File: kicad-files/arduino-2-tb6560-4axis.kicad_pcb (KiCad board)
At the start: 2 copper layers, 55.9 x 63.5 mm, 16 parts, among them J1 DB25_Female_MountingHoles, J2 Conn_01x03_Male, J3 Conn_01x02_Male, J4 Conn_01x02_Male, J5 Conn_01x03_Male, J6 Conn_01x02_Male, J7 Conn_01x03_Male, Q1 2N3904

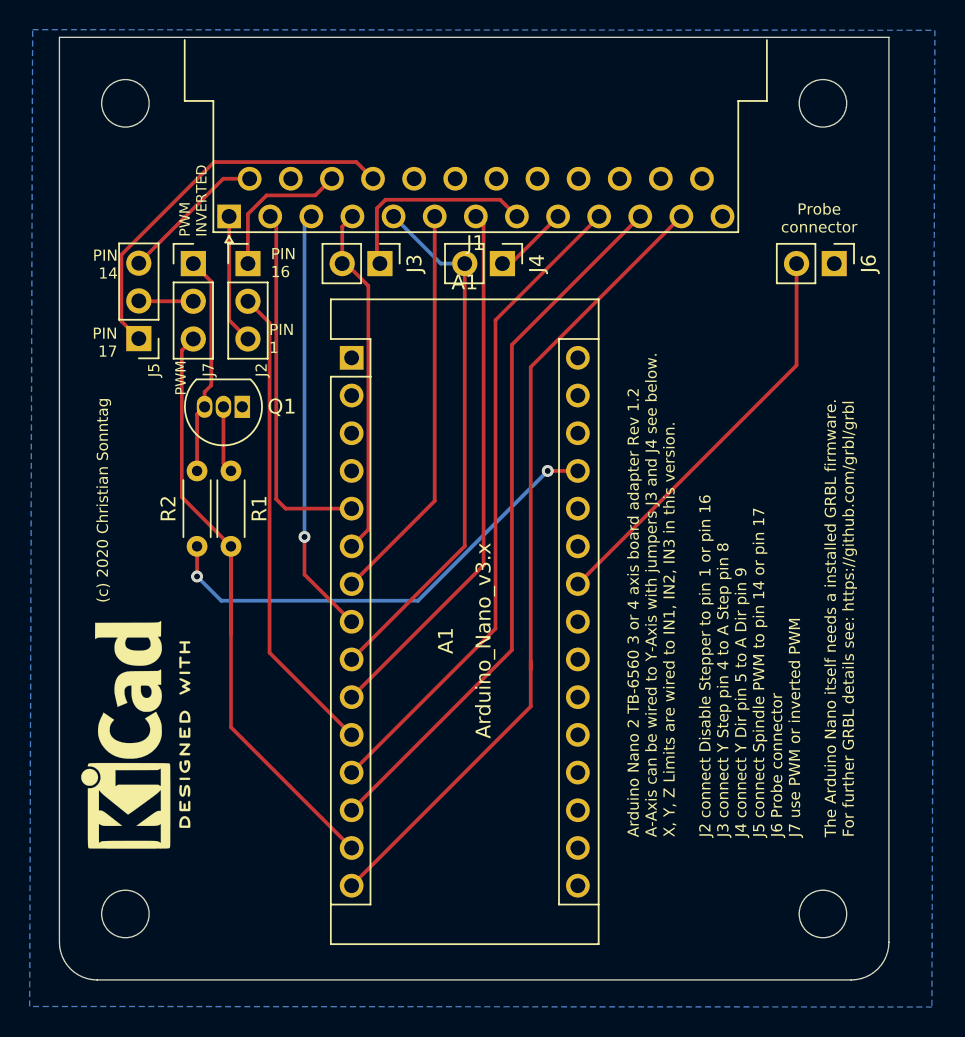
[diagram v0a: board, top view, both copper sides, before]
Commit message: added push buttons and jumper header for feed hold and cycle start/resume.
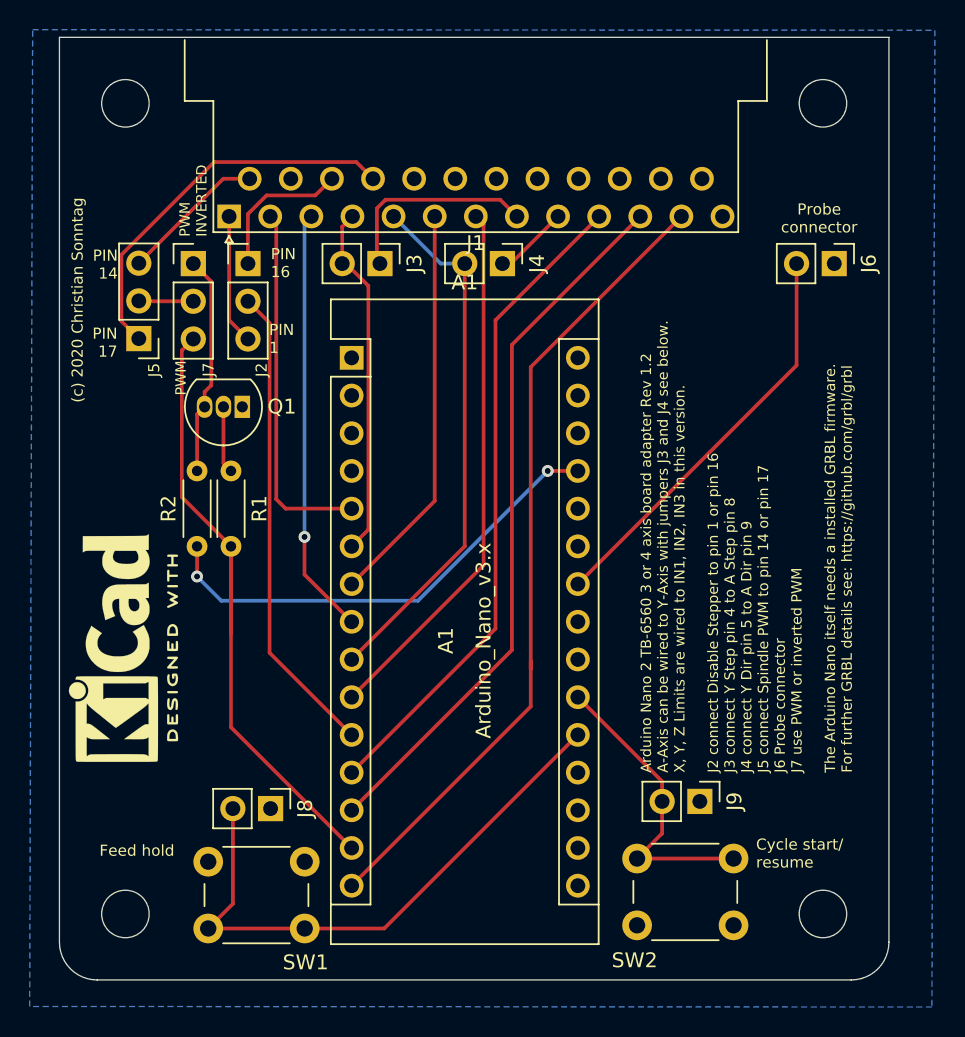
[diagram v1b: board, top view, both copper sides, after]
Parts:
- added J8: Conn_01x02_Male, Connector_PinHeader_2.54mm:PinHeader_1x02_P2.54mm_Vertical, F.Cu at (140.6, 96.4)
- added J9: Conn_01x02_Male, Connector_PinHeader_2.54mm:PinHeader_1x02_P2.54mm_Vertical, F.Cu at (169.5, 95.9)
- added SW1: SW_Push, Button_Switch_THT:SW_PUSH_6mm_H7.3mm, F.Cu at (142.9, 104.5)
- added SW2: SW_Push, Button_Switch_THT:SW_PUSH_6mm_H7.3mm, F.Cu at (165.3, 99.8)
- moved REF** 5.90 mm to (130.0, 85.6)
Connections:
- A1 pad 20: Net-(A1-Pad20) -> FEED_HOLD
- A1 pad 21: Net-(A1-Pad21) -> CYCLE_START_RESUME
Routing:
- net FEED_HOLD: track 0.00 -> 39.1 mm
- net CYCLE_START_RESUME: track 0.00 -> 20.4 mm
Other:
- board text added: "Cycle start/ resume"
- board text added: "Feed hold"

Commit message: more ideas for rev 1.3
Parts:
- added D1: LED, LED_THT:LED_D5.0mm, F.Cu at (129.0, 93.1)
- added D2: LED, LED_THT:LED_D5.0mm, F.Cu at (129.0, 86.5)
- added D3: LED, LED_THT:LED_D5.0mm, F.Cu at (129.0, 79.9)
- added R3: 1k Ohm, Resistor_THT:R_Axial_DIN0204_L3.6mm_D1.6mm_P5.08mm_Horizontal, F.Cu at (133.1, 75.6)
- added R4: 1k Ohm, Resistor_THT:R_Axial_DIN0204_L3.6mm_D1.6mm_P5.08mm_Horizontal, F.Cu at (130.9, 75.6)
- added R5: 1k Ohm, Resistor_THT:R_Axial_DIN0204_L3.6mm_D1.6mm_P5.08mm_Horizontal, F.Cu at (128.7, 75.6)
- moved REF** 25.4 mm to (152.5, 73.8)
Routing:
- net Z_STEP: track 27.1 -> 48.9 mm, vias 0 -> 1
- net Net-(D1-Pad1): track 0.00 -> 19.2 mm
- net Y_STEP: track 23.9 -> 42.5 mm, vias 0 -> 1
- net Net-(D2-Pad1): track 0.00 -> 11.7 mm
- net X_STEP: track 24.3 -> 35.6 mm, vias 0 -> 2
- net Net-(D3-Pad1): track 0.00 -> 4.47 mm
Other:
- board text added: "Arduino Nano 2 TB-6560 3 or 4 axis board adapter Rev 1.3 A-Axis can be wired to Y-Axis with jumpers J3 and J4 see below. X, Y, Z Limits are wired to IN1, IN2, IN3 in this version. J2 connect Disable Stepper to pin 1 or pin 16 J3 connect Y Step pin 4 to A Step pin 8 J4 connect Y Dir pin 5 to A Dir pin 9 J5 connect Spindle PWM to pin 14 or pin 17 J6 Probe connector J7 use PWM or inverted PWM The Ar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"
- board text added: "USB"
- board text added: "X"
- board text added: "Y"
- board text added: "Z"
- board text removed: "Arduino Nano 2 TB-6560 3 or 4 axis board adapter Rev 1.2 A-Axis can be wired to Y-Axis with jumpers J3 and J4 see below. X, Y, Z Limits are wired to IN1, IN2, IN3 in this version. J2 connect Disable Stepper to pin 1 or pin 16 J3 connect Y Step pin 4 to A Step pin 8 J4 connect Y Dir pin 5 to A Dir pin 9 J5 connect Spindle PWM to pin 14 or pin 17 J6 Probe connector J7 use PWM or inverted PWM The Ar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"

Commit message: rev. 1.4. fix wrong led orientation. fix wrong resistor footprint. reroute affected tracks.
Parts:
- R1, R2, R3, R4, R5: footprint Resistor_THT:R_Axial_DIN0204_L3.6mm_D1.6mm_P5.08mm_Horizontal -> Resistor_THT:R_Axial_DIN0207_L6.3mm_D2.5mm_P7.62mm_Horizontal
- moved R3 15.9 mm to (135.1, 91.4), turned to 0 degrees
- moved R4 13.4 mm to (135.1, 88.2), turned to 0 degrees
- moved R5 11.5 mm to (135.1, 85.1), turned to 0 degrees
- moved R1 1.57 mm to (139.0, 72.6)
- moved R2 1.48 mm to (136.0, 80.2)
- moved Q1 0.75 mm to (138.6, 68.6)
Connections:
- D1 pad 1: Net-(D1-Pad1) -> GND
- D1 pad 2: GND -> Net-(D1-Pad2)
- D2 pad 1: Net-(D2-Pad1) -> GND
- D2 pad 2: GND -> Net-(D2-Pad2)
- D3 pad 1: Net-(D3-Pad1) -> GND
- D3 pad 2: GND -> Net-(D3-Pad2)
- R3 pad 1: Net-(D1-Pad1) -> Net-(D1-Pad2)
- R4 pad 1: Net-(D2-Pad1) -> Net-(D2-Pad2)
- R5 pad 1: Net-(D3-Pad1) -> Net-(D3-Pad2)
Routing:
- net Net-(D1-Pad1): track 19.2 -> 0.00 mm
- net Z_STEP: track 48.9 -> 34.6 mm
- net Net-(D2-Pad1): track 11.7 -> 0.00 mm
- net Net-(D3-Pad2): track 0.00 -> 7.53 mm
- net SPINDLE_PWM: track 44.4 -> 38.5 mm
- net X_STEP: track 35.6 -> 40.2 mm, vias 2 -> 0
- net Net-(D3-Pad1): track 4.47 -> 0.00 mm
- net Y_STEP: track 42.5 -> 38.2 mm, vias 1 -> 0
- net Net-(D2-Pad2): track 0.00 -> 4.26 mm
- net Net-(D1-Pad2): track 0.00 -> 4.26 mm
- net DISABLE_STEPPER: track 32.1 -> 35.9 mm
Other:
- board text added: "Arduino Nano 2 TB-6560 3 or 4 axis board adapter Rev 1.4 A-Axis can be wired to Y-Axis with jumpers J3 and J4 see below. X, Y, Z Limits are wired to IN1, IN2, IN3 in this version. J2 connect Disable Stepper to pin 1 or pin 16 J3 connect Y Step pin 4 to A Step pin 8 J4 connect Y Dir pin 5 to A Dir pin 9 J5 connect Spindle PWM to pin 14 or pin 17 J6 Probe connector J7 use PWM or inverted PWM The Ar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"
- board text removed: "Arduino Nano 2 TB-6560 3 or 4 axis board adapter Rev 1.3 A-Axis can be wired to Y-Axis with jumpers J3 and J4 see below. X, Y, Z Limits are wired to IN1, IN2, IN3 in this version. J2 connect Disable Stepper to pin 1 or pin 16 J3 connect Y Step pin 4 to A Step pin 8 J4 connect Y Dir pin 5 to A Dir pin 9 J5 connect Spindle PWM to pin 14 or pin 17 J6 Probe connector J7 use PWM or inverted PWM The Ar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"
